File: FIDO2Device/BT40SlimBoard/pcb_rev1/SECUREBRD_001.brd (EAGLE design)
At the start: 30 x 30 mm, 31 parts, among them CN1 2137160001, CN2 IF_5PIN_H, CN3 IF_4PIN_SOL, SW1 SKRPACE010, SW2 SKRPACE010, SW3 SKTADAE010, U1 BT40, U2 ADP122ACPZ-3.3-R7

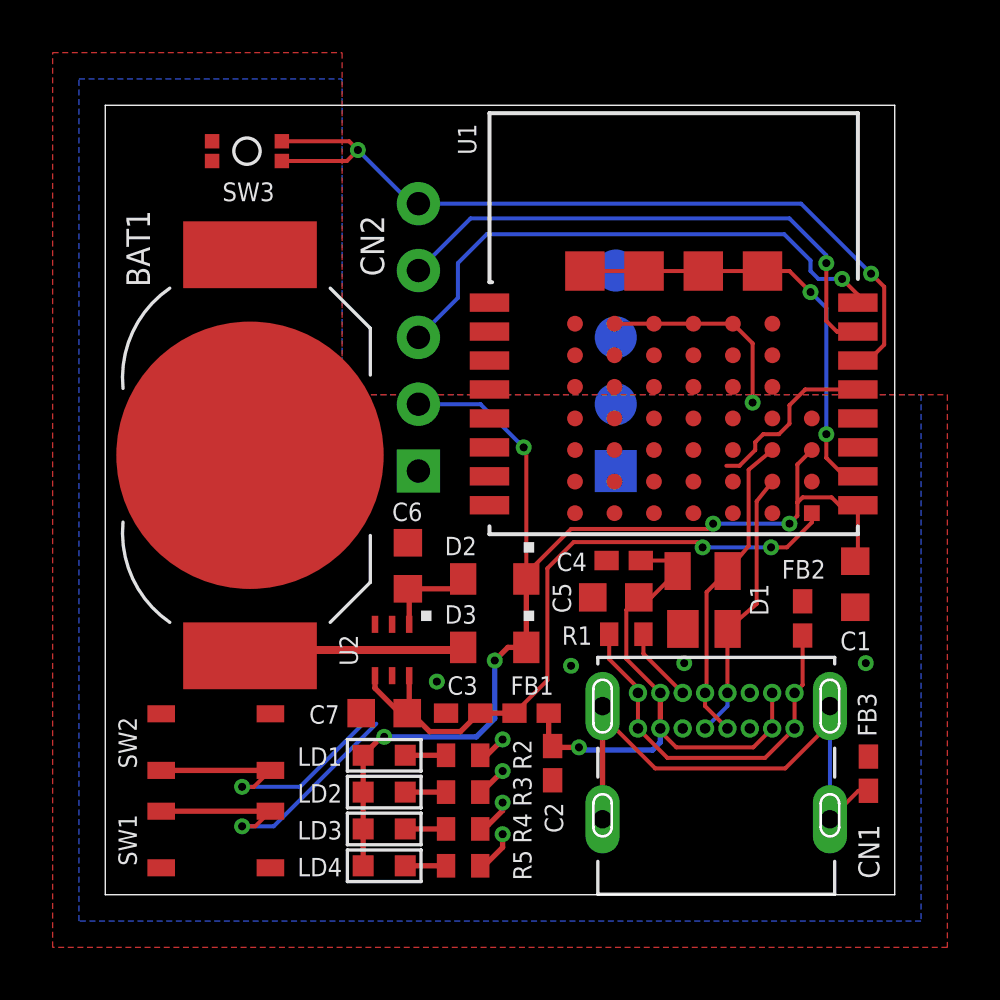
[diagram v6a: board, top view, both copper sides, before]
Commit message: 配線レイアウトを作成
・LEDの配線を作成
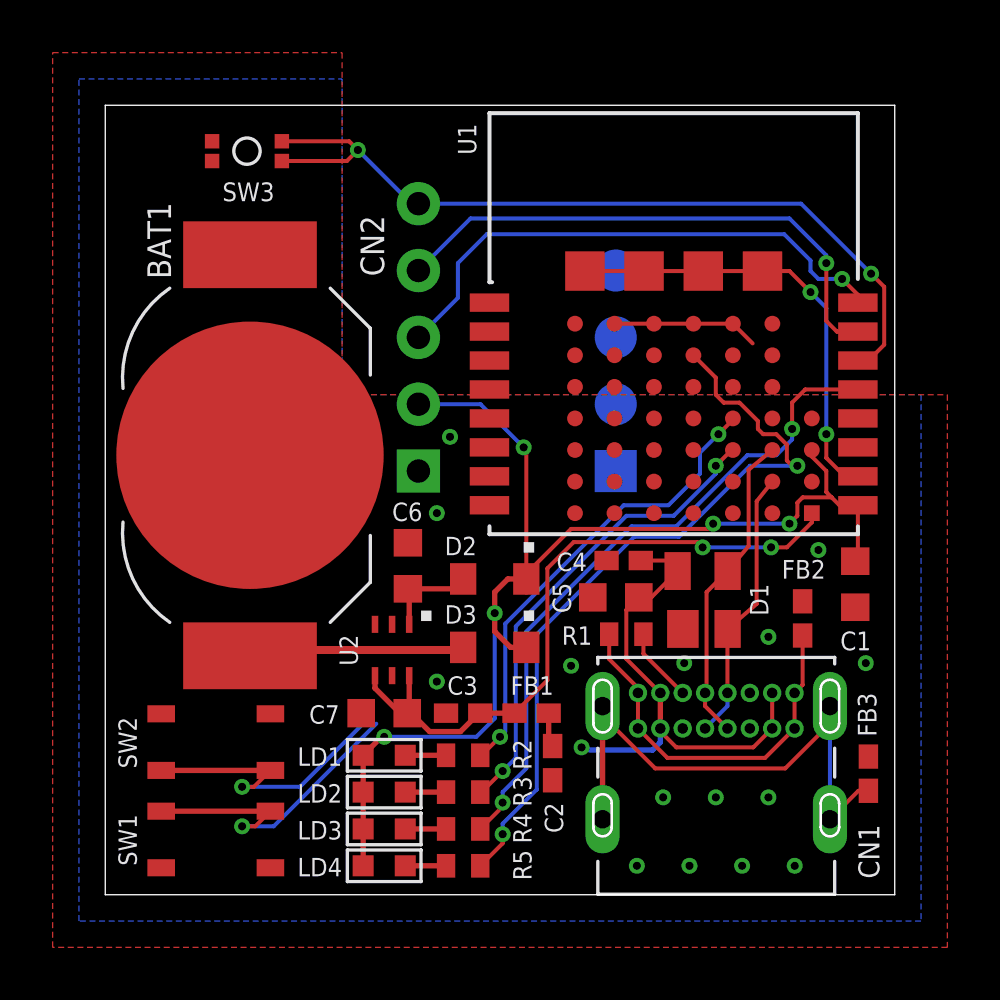
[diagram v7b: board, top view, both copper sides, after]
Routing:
- net LED4: track 1.64 -> 28.8 mm, vias 1 -> 2
- net LED3: track 8.31 -> 25.5 mm, vias 1 -> 2
- net LED2: track 1.18 -> 18.1 mm, vias 1 -> 2
- net LED1: track 1.10 -> 17.8 mm, vias 1 -> 2
- net VDD_NRF: track 45.0 -> 47.4 mm
- net 0V: track 24.8 -> 22.5 mm, vias 7 -> 17
- net VBUS: track 21.7 -> 20.3 mm

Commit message: 配線レイアウトを作成
・スイッチ、調査用信号（AIN／TXD）の配線を作成
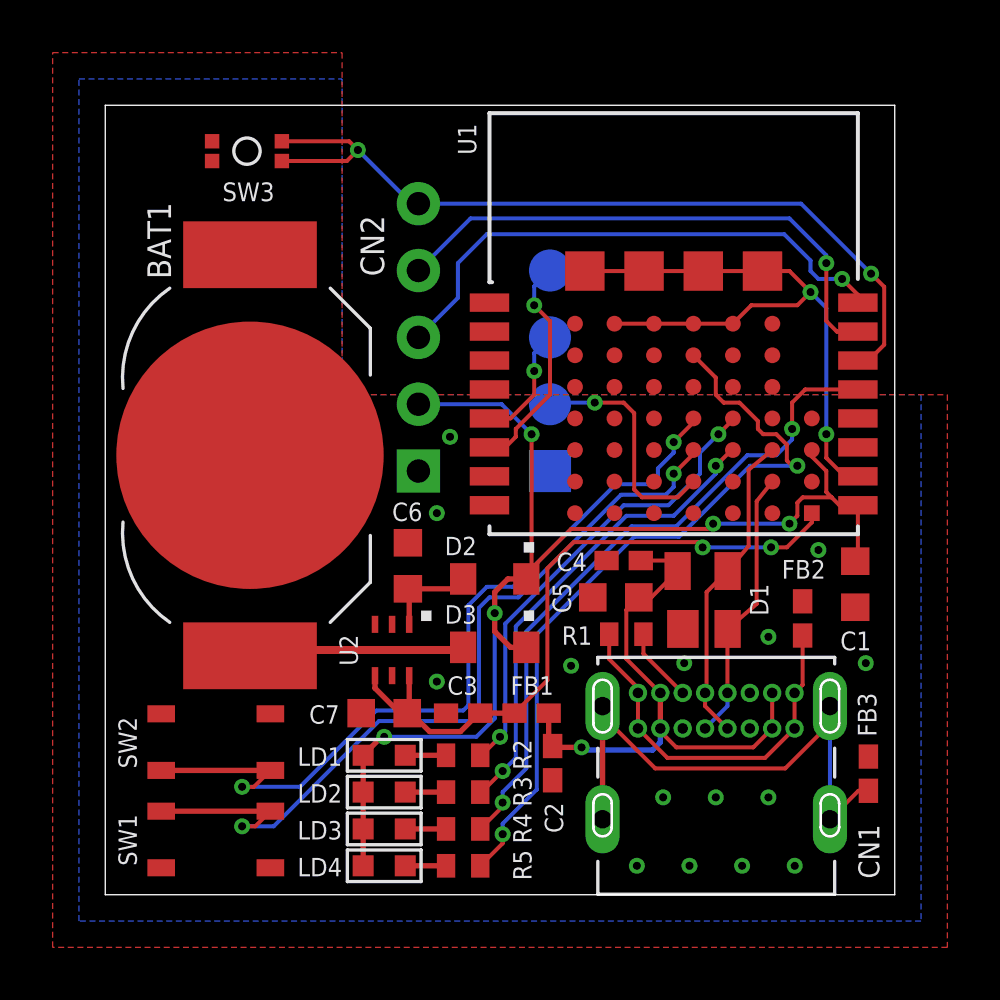
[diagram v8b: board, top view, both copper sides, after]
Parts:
- moved CN3 2.50 mm to (16.9, 16.1)
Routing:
- net SW2: track 11.4 -> 31.2 mm, vias 1 -> 2
- net SW1: track 12.2 -> 31.3 mm, vias 1 -> 2
- net TXD: track 0.00 -> 8.91 mm, vias 0 -> 1
- net AIN1: track 0.00 -> 8.52 mm, vias 0 -> 1
- net AIN0: track 0.00 -> 4.50 mm, vias 0 -> 1
- net 0V: track 22.5 -> 24.9 mm
- net VBUS: track 20.3 -> 21.7 mm
- net VDD_NRF: track 47.4 -> 48.0 mm
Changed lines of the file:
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@@
 <text x="13" y="23.7" size="0.6" layer="22" rot="R270" align="bottom-center">PCLK</text>
 <text x="13" y="26.2" size="0.6" layer="22" rot="R270" align="bottom-center">RST</text>
-<text x="18.3" y="23.7" size="0.6" layer="22" rot="MR270" align="bottom-center">AIN1</text>
-<text x="18.3" y="21.2" size="0.6" layer="22" rot="MR270" align="bottom-center">AIN0</text>
-<text x="18.3" y="18.6" size="0.6" layer="22" rot="MR270" align="bottom-center">TXD</text>
-<text x="18.3" y="16.1" size="0.6" layer="22" rot="MR270" align="bottom-center">GND</text>
+<text x="15.8" y="23.7" size="0.6" layer="22" rot="MR270" align="bottom-center">AIN1</text>
+<text x="15.8" y="21.2" size="0.6" layer="22" rot="MR270" align="bottom-center">AIN0</text>
+<text x="15.8" y="18.6" size="0.6" layer="22" rot="MR270" align="bottom-center">TXD</text>
+<text x="15.8" y="16.1" size="0.6" layer="22" rot="MR270" align="bottom-center">GND</text>
 </plain>
 <attributes>
@@
 <attribute name="VALUE" x="13.17" y="14.83" size="0.889" layer="27" ratio="11" rot="R90" align="top-left"/>
 </element>
-<element name="CN3" library="Connectors" package="SOLPAD_4PIN" value="IF_4PIN_SOL" x="19.4" y="16.1" rot="MR90"/>
+<element name="CN3" library="Connectors" package="SOLPAD_4PIN" value="IF_4PIN_SOL" x="16.9" y="16.1" rot="MR90"/>
 </elements>
 <signals>
@@
 <via x="28.9" y="8.8" extent="1-16" drill="0.3048"/>
 <via x="27.4" y="17.5" extent="1-16" drill="0.3048"/>
-<wire x1="23.85" y1="21.7" x2="24.6" y2="20.95" width="0.1524" layer="1"/>
 <wire x1="22.35" y1="21.7" x2="23.85" y2="21.7" width="0.1524" layer="1"/>
 <wire x1="22.35" y1="21.7" x2="20.85" y2="21.7" width="0.1524" layer="1"/>
@@
 <wire x1="27.4" y1="16.6" x2="28.1" y2="15.9" width="0.1524" layer="1"/>
 <wire x1="28.1" y1="15.9" x2="28.6" y2="15.9" width="0.1524" layer="1"/>
-<wire x1="20.475" y1="23.7" x2="20.85" y2="21.7" width="0" layer="19" extent="1-1"/>
+<wire x1="23.85" y1="21.7" x2="24.55" y2="22.4" width="0.1524" layer="1"/>
+<wire x1="24.55" y1="22.4" x2="26.3" y2="22.4" width="0.1524" layer="1"/>
+<wire x1="26.3" y1="22.4" x2="26.8" y2="22.9" width="0.1524" layer="1"/>
 </signal>
 <signal name="VBUS_NRF">
@@
 <wire x1="9.8" y1="5.3" x2="10.5" y2="6" width="0.2032" layer="1"/>
 <wire x1="10.5" y1="6" x2="10.6" y2="6" width="0.2032" layer="1"/>
-<via x="15.9" y="17" extent="1-16" drill="0.3048"/>
-<wire x1="16" y1="12" x2="16" y2="16.9" width="0.1524" layer="1"/>
-<wire x1="16" y1="16.9" x2="15.9" y2="17" width="0.1524" layer="1"/>
-<wire x1="11.9" y1="18.64" x2="14.26" y2="18.64" width="0.1524" layer="16"/>
-<wire x1="14.26" y1="18.64" x2="15.9" y2="17" width="0.1524" layer="16"/>
+<via x="16.2" y="17.5" extent="1-16" drill="0.3048"/>
+<wire x1="11.9" y1="18.64" x2="15.06" y2="18.64" width="0.1524" layer="16"/>
 <via x="23.1" y="14.1" extent="1-16" drill="0.3048"/>
 <via x="26" y="14.1" extent="1-16" drill="0.3048"/>
@@
 <wire x1="27.4" y1="16.1" x2="27.4" y2="15.3" width="0.1524" layer="1"/>
 <wire x1="27.4" y1="15.3" x2="27.6" y2="15.1" width="0.1524" layer="1"/>
+<wire x1="15.06" y1="18.64" x2="16.2" y2="17.5" width="0.1524" layer="16"/>
+<wire x1="16.2" y1="17.5" x2="16.2" y2="12.2" width="0.1524" layer="1"/>
+<wire x1="16.2" y1="12.2" x2="16" y2="12" width="0.1524" layer="1"/>
 </signal>
 <signal name="SW2">
@@
 <via x="5.2" y="4.1" extent="1-16" drill="0.3048"/>
 <wire x1="5.2" y1="4.1" x2="7.4" y2="4.1" width="0.1524" layer="16"/>
-<wire x1="7.4" y1="4.1" x2="10" y2="6.7" width="0.1524" layer="16"/>
+<wire x1="7.4" y1="4.1" x2="10.3" y2="7" width="0.1524" layer="16"/>
 <wire x1="5.2" y1="4.1" x2="5.65" y2="4.1" width="0.1524" layer="1"/>
 <wire x1="5.65" y1="4.1" x2="6.275" y2="4.725" width="0.1524" layer="1"/>
-<wire x1="10" y1="6.7" x2="22.35" y2="18.1" width="0" layer="19" extent="1-16"/>
+<via x="21.6" y="17.2" extent="1-16" drill="0.3048"/>
+<wire x1="13.8" y1="7.2" x2="13.8" y2="11" width="0.1524" layer="16"/>
+<wire x1="13.8" y1="11" x2="14.5" y2="11.7" width="0.1524" layer="16"/>
+<wire x1="14.5" y1="11.7" x2="15.5" y2="11.7" width="0.1524" layer="16"/>
+<wire x1="15.5" y1="11.7" x2="19.4" y2="15.6" width="0.1524" layer="16"/>
+<wire x1="10.3" y1="7" x2="13.6" y2="7" width="0.1524" layer="16"/>
+<wire x1="13.6" y1="7" x2="13.8" y2="7.2" width="0.1524" layer="16"/>
+<wire x1="19.4" y1="15.6" x2="20.7" y2="15.6" width="0.1524" layer="16"/>
+<wire x1="20.7" y1="15.6" x2="21" y2="15.9" width="0.1524" layer="16"/>
+<wire x1="21" y1="15.9" x2="21" y2="16.2" width="0.1524" layer="16"/>
+<wire x1="21" y1="16.2" x2="21.6" y2="16.8" width="0.1524" layer="16"/>
+<wire x1="21.6" y1="16.8" x2="21.6" y2="17.2" width="0.1524" layer="16"/>
+<wire x1="21.6" y1="17.2" x2="22.35" y2="17.95" width="0.1524" layer="1"/>
+<wire x1="22.35" y1="17.95" x2="22.35" y2="18.1" width="0.1524" layer="1"/>
 </signal>
 <signal name="SW1">
@@
 <contactref element="U1" pad="C4"/>
 <wire x1="2.125" y1="3.175" x2="6.275" y2="3.175" width="0.2032" layer="1"/>
-<wire x1="6.4" y1="2.6" x2="10.3" y2="6.5" width="0.1524" layer="16"/>
+<wire x1="6.4" y1="2.6" x2="10.4" y2="6.6" width="0.1524" layer="16"/>
 <wire x1="6.4" y1="2.6" x2="5.2" y2="2.6" width="0.1524" layer="16"/>
 <via x="5.2" y="2.6" extent="1-16" drill="0.3048"/>
 <wire x1="5.2" y1="2.6" x2="5.7" y2="2.6" width="0.1524" layer="1"/>
 <wire x1="5.7" y1="2.6" x2="6.275" y2="3.175" width="0.1524" layer="1"/>
-<wire x1="10.3" y1="6.5" x2="22.35" y2="16.9" width="0" layer="19" extent="1-16"/>
+<via x="21.6" y="16" extent="1-16" drill="0.3048"/>
+<wire x1="14.2" y1="6.9" x2="14.2" y2="10.9" width="0.1524" layer="16"/>
+<wire x1="14.2" y1="10.9" x2="14.6" y2="11.3" width="0.1524" layer="16"/>
+<wire x1="14.6" y1="11.3" x2="15.7" y2="11.3" width="0.1524" layer="16"/>
+<wire x1="15.7" y1="11.3" x2="19.6" y2="15.2" width="0.1524" layer="16"/>
+<wire x1="10.4" y1="6.6" x2="13.9" y2="6.6" width="0.1524" layer="16"/>
+<wire x1="13.9" y1="6.6" x2="14.2" y2="6.9" width="0.1524" layer="16"/>
+<wire x1="19.6" y1="15.2" x2="21.3" y2="15.2" width="0.1524" layer="16"/>
+<wire x1="21.3" y1="15.2" x2="21.6" y2="15.5" width="0.1524" layer="16"/>
+<wire x1="21.6" y1="15.5" x2="21.6" y2="16" width="0.1524" layer="16"/>
+<wire x1="21.6" y1="16" x2="22.35" y2="16.75" width="0.1524" layer="1"/>
+<wire x1="22.35" y1="16.75" x2="22.35" y2="16.9" width="0.1524" layer="1"/>
 </signal>
 <signal name="RESET">
@@
 <wire x1="16.85" y1="5.8" x2="17" y2="5.65" width="0.2032" layer="1"/>
 <wire x1="17" y1="5.65" x2="17.05" y2="5.6" width="0.2032" layer="1"/>
-<wire x1="18.4" y1="5.5" x2="20.8" y2="5.5" width="0.2032" layer="16"/>
+<wire x1="18.2" y1="5.5" x2="20.8" y2="5.5" width="0.2032" layer="16"/>
 <wire x1="20.8" y1="5.5" x2="21.0928" y2="5.7928" width="0.2032" layer="16"/>
 <wire x1="21.0928" y1="6.3188" x2="21.0928" y2="5.7928" width="0.2032" layer="16"/>
@@
 <wire x1="20.35" y1="12.7" x2="21.35" y2="12.7" width="0.1524" layer="1"/>
 <wire x1="21.35" y1="12.7" x2="21.75" y2="12.3" width="0.1524" layer="1"/>
-<wire x1="18.4" y1="5.5" x2="18.1" y2="5.6" width="0" layer="19" extent="16-16"/>
-<wire x1="17.05" y1="5.6" x2="18.1" y2="5.6" width="0" layer="19" extent="1-1"/>
+<wire x1="17.05" y1="5.6" x2="18.1" y2="5.6" width="0.2032" layer="1"/>
+<wire x1="18.2" y1="5.5" x2="18.1" y2="5.6" width="0.2032" layer="16"/>
 </signal>
 <signal name="USB_GND">
@@
 <contactref element="U1" pad="C5"/>
 <contactref element="CN3" pad="2"/>
-<wire x1="19.4" y1="18.64" x2="22.35" y2="15.7" width="0" layer="19" extent="1-16"/>
+<wire x1="22.35" y1="15.7" x2="21.75" y2="15.1" width="0.1524" layer="1"/>
+<wire x1="21.75" y1="15.1" x2="20.4" y2="15.1" width="0.1524" layer="1"/>
+<via x="18.6" y="18.7" extent="1-16" drill="0.3048"/>
+<wire x1="18.6" y1="18.7" x2="16.96" y2="18.7" width="0.1524" layer="16"/>
+<wire x1="16.96" y1="18.7" x2="16.9" y2="18.64" width="0.1524" layer="16"/>
+<wire x1="20.4" y1="15.1" x2="20.1" y2="15.4" width="0.1524" layer="1"/>
+<wire x1="20.1" y1="15.4" x2="20.1" y2="18.3" width="0.1524" layer="1"/>
+<wire x1="20.1" y1="18.3" x2="19.7" y2="18.7" width="0.1524" layer="1"/>
+<wire x1="19.7" y1="18.7" x2="18.6" y2="18.7" width="0.1524" layer="1"/>
 </signal>
 <signal name="AIN0">
 <contactref element="U1" pad="5"/>
 <contactref element="CN3" pad="3"/>
-<wire x1="14.6" y1="18.1" x2="19.4" y2="21.18" width="0" layer="19" extent="1-16"/>
+<via x="16.3" y="19.9" extent="1-16" drill="0.3048"/>
+<wire x1="16.9" y1="21.18" x2="16.3" y2="20.58" width="0.1524" layer="16"/>
+<wire x1="16.3" y1="20.58" x2="16.3" y2="19.9" width="0.1524" layer="16"/>
+<wire x1="14.6" y1="18.1" x2="15.4" y2="18.1" width="0.1524" layer="1"/>
+<wire x1="15.4" y1="18.1" x2="16.3" y2="19" width="0.1524" layer="1"/>
+<wire x1="16.3" y1="19" x2="16.3" y2="19.9" width="0.1524" layer="1"/>
 </signal>
 <signal name="AIN1">
 <contactref element="U1" pad="6"/>
 <contactref element="CN3" pad="4"/>
-<wire x1="14.6" y1="17" x2="19.4" y2="23.72" width="0" layer="19" extent="1-16"/>
+<wire x1="14.6" y1="17" x2="15.2" y2="17" width="0.1524" layer="1"/>
+<wire x1="15.2" y1="17" x2="15.6" y2="17.4" width="0.1524" layer="1"/>
+<wire x1="15.6" y1="17.4" x2="15.6" y2="17.7" width="0.1524" layer="1"/>
+<wire x1="15.6" y1="17.7" x2="16.9" y2="19" width="0.1524" layer="1"/>
+<via x="16.3" y="22.4" extent="1-16" drill="0.3048"/>
+<wire x1="16.9" y1="19" x2="16.9" y2="21.8" width="0.1524" layer="1"/>
+<wire x1="16.9" y1="21.8" x2="16.3" y2="22.4" width="0.1524" layer="1"/>
+<wire x1="16.9" y1="23.72" x2="16.3" y2="23.12" width="0.1524" layer="16"/>
+<wire x1="16.3" y1="23.12" x2="16.3" y2="22.4" width="0.1524" layer="16"/>
 </signal>
 <signal name="N$2">
